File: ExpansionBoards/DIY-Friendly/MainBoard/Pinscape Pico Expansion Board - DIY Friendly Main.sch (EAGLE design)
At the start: 111 parts, among them IC1 UCC27524P, IC10 ULN2803A, IC11 SN74HC165N, IC12 SN74HC165N, IC13 SN74HC74NE4, IC14 PC827, IC15 S-80833CLY, IC16 SN74HC165N, IC18 SN74HC165N, IC2 UCC27524P, IC3 UCC27524P, IC4 UCC27524P, IC5 UCC27524P, IC6 UCC27524P, IC7 ULN2803A, IC8 ULN2803A, IC9 ULN2803A, J1 30316-6002HB, J10 215079-4, J11 640454-2, J13 640445-2, J14 SSQ-108-02-T-S-RA, J2 640445-6, J3 640445-5, J4 640445-9, J5 1-640456-0, J6 1-640456-0, J7 1-640456-0, J8 1-640456-0, J9 30308-6002HB, Q1 FDPF085N10A, Q10 FDPF085N10A, Q11 FDPF085N10A, Q12 FDPF085N10A, Q13 BC337-25, Q15 2N5195G, Q16 2N2222A, Q2 FDPF085N10A, Q3 FDPF085N10A, Q4 FDPF085N10A, Q5 FDPF085N10A, Q6 FDPF085N10A, Q7 FDPF085N10A, Q8 FDPF085N10A, Q9 FDPF085N10A

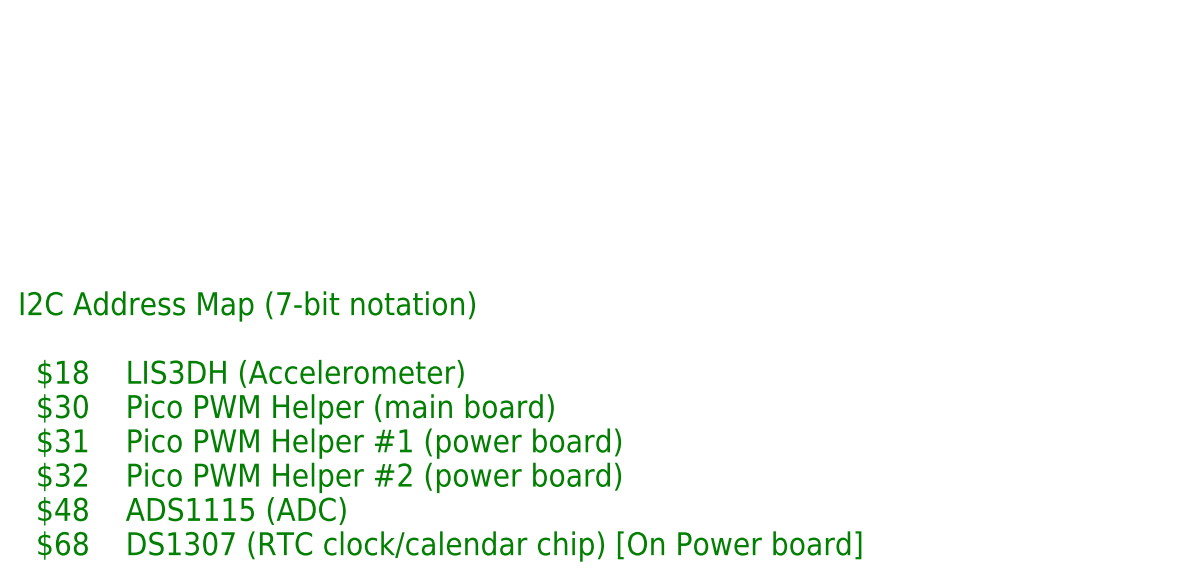
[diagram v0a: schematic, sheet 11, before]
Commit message: PCB parts lists (BOMs); power distro board edits
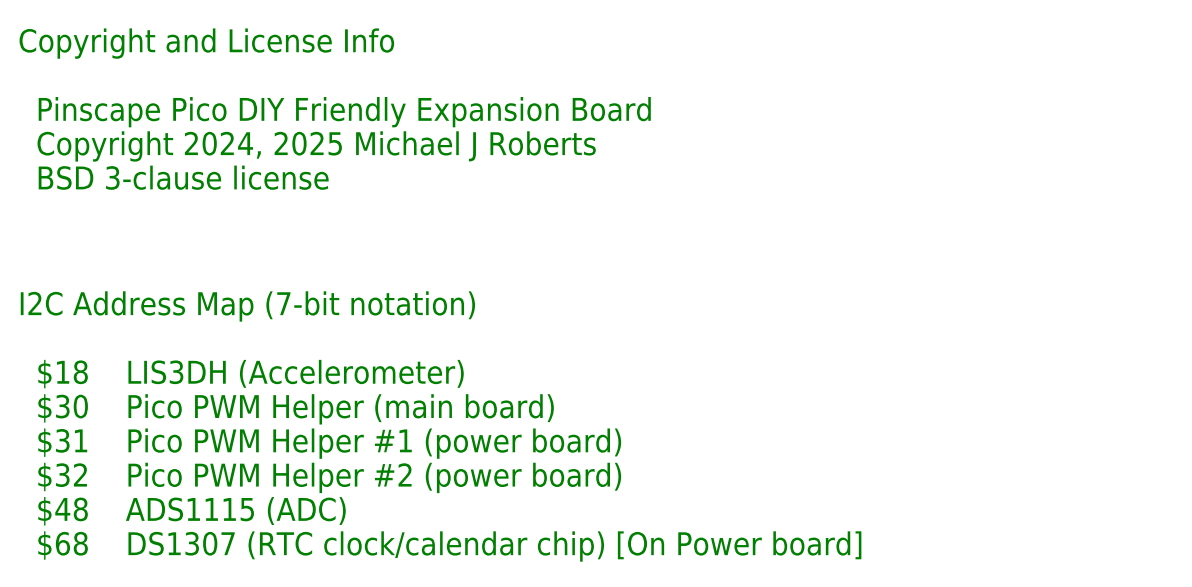
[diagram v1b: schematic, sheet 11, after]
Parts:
- C1, C10, C11, C13, C15, C18, C19, C3, C5, C7, C9: PARTNO 21RZ310-RC -> K104K15X7RF5TL2
- R10, R11: PARTNO 660-MFS1/4DCT52R47R0 -> MFR25SFTE52-10R
- R12, R13, R20, R22: PARTNO 660-MFS1/4DCT52R47R0 -> mfr-12frrf52-10k
- R26: PARTNO 660-MFS1/4DCT52R47R0 -> MF0204FTE52-1K
- R29, R30: PARTNO 660-MFS1/4DCT52R47R0 -> MFR25SFRF52-15K
- R9: PARTNO 660-MFS1/4DCT52R47R0 -> MFR-12FTE52-100R
- S1, S2: value (none) -> B3F-1000
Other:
- note added: "Copyright and License Info Pinscape Pico DIY Friendly Expansion Board Copyright 2024, 2025 Michael J Roberts BSD 3-clause license"
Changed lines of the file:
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@@
 <part name="GND47" library="supply1" deviceset="GND" device=""/>
 <part name="PICO1" library="RaspberryPi_Pico" deviceset="RPI_PICO_NO_DEBUG" device=""/>
-<part name="S1" library="switch-omron" deviceset="10-XX" device=""/>
+<part name="S1" library="switch-omron" deviceset="10-XX" device="" value="B3F-1000"/>
 <part name="JP1" library="pinhead" deviceset="PINHD-1X6" device=""/>
 <part name="JP2" library="pinhead" deviceset="PINHD-1X6" device=""/>
@@
 </part>
 <part name="C1" library="rcl" deviceset="C-US" device="025-024X044" value="100nF">
-<attribute name="PARTNO" value="21RZ310-RC"/>
+<attribute name="PARTNO" value="K104K15X7RF5TL2"/>
 </part>
 <part name="C2" library="rcl" deviceset="C-US" device="025-024X044" value="4.7uF">
@@
 </part>
 <part name="C3" library="rcl" deviceset="C-US" device="025-024X044" value="100nF">
-<attribute name="PARTNO" value="21RZ310-RC"/>
+<attribute name="PARTNO" value="K104K15X7RF5TL2"/>
 </part>
 <part name="C4" library="rcl" deviceset="C-US" device="025-024X044" value="4.7uF">
@@
 </part>
 <part name="C5" library="rcl" deviceset="C-US" device="025-024X044" value="100nF">
-<attribute name="PARTNO" value="21RZ310-RC"/>
+<attribute name="PARTNO" value="K104K15X7RF5TL2"/>
 </part>
 <part name="C6" library="rcl" deviceset="C-US" device="025-024X044" value="4.7uF">
@@
 </part>
 <part name="C7" library="rcl" deviceset="C-US" device="025-024X044" value="100nF">
-<attribute name="PARTNO" value="21RZ310-RC"/>
+<attribute name="PARTNO" value="K104K15X7RF5TL2"/>
 </part>
 <part name="C8" library="rcl" deviceset="C-US" device="025-024X044" value="4.7uF">
@@
 <part name="D1" library="SamacSys_Parts" deviceset="SB140-T" device=""/>
 <part name="R9" library="resistor" deviceset="R-US_" device="0204/7" value="100R">
-<attribute name="PARTNO" value="660-MFS1/4DCT52R47R0"/>
+<attribute name="PARTNO" value="MFR-12FTE52-100R"/>
 </part>
 <part name="LED2" library="SamacSys_Parts" deviceset="521-8559F" device=""/>
 <part name="R10" library="resistor" deviceset="R-US_" device="0204/7" value="10R">
-<attribute name="PARTNO" value="660-MFS1/4DCT52R47R0"/>
+<attribute name="PARTNO" value="MFR25SFTE52-10R"/>
 </part>
 <part name="R11" library="resistor" deviceset="R-US_" device="0204/7" value="10R">
-<attribute name="PARTNO" value="660-MFS1/4DCT52R47R0"/>
+<attribute name="PARTNO" value="MFR25SFTE52-10R"/>
 </part>
 <part name="R12" library="resistor" deviceset="R-US_" device="0204/7" value="10K">
-<attribute name="PARTNO" value="660-MFS1/4DCT52R47R0"/>
+<attribute name="PARTNO" value="mfr-12frrf52-10k"/>
 </part>
 <part name="R13" library="resistor" deviceset="R-US_" device="0204/7" value="10K">
-<attribute name="PARTNO" value="660-MFS1/4DCT52R47R0"/>
+<attribute name="PARTNO" value="mfr-12frrf52-10k"/>
 </part>
 <part name="C9" library="rcl" deviceset="C-US" device="025-024X044" value="100nF">
-<attribute name="PARTNO" value="21RZ310-RC"/>
+<attribute name="PARTNO" value="K104K15X7RF5TL2"/>
 </part>
 <part name="IC7" library="uln-udn" deviceset="ULN2803A" device="" value="ULN2803A"/>
@@
 </part>
 <part name="C11" library="rcl" deviceset="C-US" device="025-024X044" value="100nF">
-<attribute name="PARTNO" value="21RZ310-RC"/>
+<attribute name="PARTNO" value="K104K15X7RF5TL2"/>
 </part>
 <part name="C12" library="rcl" deviceset="C-US" device="025-024X044" value="4.7uF">
@@
 </part>
 <part name="C13" library="rcl" deviceset="C-US" device="025-024X044" value="100nF">
-<attribute name="PARTNO" value="21RZ310-RC"/>
+<attribute name="PARTNO" value="K104K15X7RF5TL2"/>
 </part>
 <part name="C14" library="rcl" deviceset="C-US" device="025-024X044" value="4.7uF">
@@
 <part name="IC15" library="SamacSys_Parts" deviceset="S-80833CLY-B2-U" device="TO92" value="S-80833CLY"/>
 <part name="C15" library="rcl" deviceset="C-US" device="025-024X044" value="100nF">
-<attribute name="PARTNO" value="21RZ310-RC"/>
+<attribute name="PARTNO" value="K104K15X7RF5TL2"/>
 </part>
 <part name="R18" library="resistor" deviceset="R-US_" device="0204/7" value="240R">
@@
 </part>
 <part name="R20" library="resistor" deviceset="R-US_" device="0204/7" value="10K">
-<attribute name="PARTNO" value="660-MFS1/4DCT52R47R0"/>
+<attribute name="PARTNO" value="mfr-12frrf52-10k"/>
 </part>
 <part name="R21" library="resistor" deviceset="R-US_" device="0204/7" value="360R">
@@
 </part>
 <part name="R22" library="resistor" deviceset="R-US_" device="0204/7" value="10K">
-<attribute name="PARTNO" value="660-MFS1/4DCT52R47R0"/>
+<attribute name="PARTNO" value="mfr-12frrf52-10k"/>
 </part>
 <part name="J13" library="SamacSys_Parts" deviceset="640445-2" device=""/>
@@
 <part name="IC11" library="SamacSys_Parts" deviceset="SN74HC165N" device=""/>
 <part name="C10" library="rcl" deviceset="C-US" device="025-024X044" value="100nF">
-<attribute name="PARTNO" value="21RZ310-RC"/>
+<attribute name="PARTNO" value="K104K15X7RF5TL2"/>
 </part>
 <part name="IC12" library="SamacSys_Parts" deviceset="SN74HC165N" device=""/>
 <part name="C18" library="rcl" deviceset="C-US" device="025-024X044" value="100nF">
-<attribute name="PARTNO" value="21RZ310-RC"/>
+<attribute name="PARTNO" value="K104K15X7RF5TL2"/>
 </part>
 <part name="IC16" library="SamacSys_Parts" deviceset="SN74HC165N" device=""/>
 <part name="C19" library="rcl" deviceset="C-US" device="025-024X044" value="100nF">
-<attribute name="PARTNO" value="21RZ310-RC"/>
+<attribute name="PARTNO" value="K104K15X7RF5TL2"/>
 </part>
 <part name="IC18" library="SamacSys_Parts" deviceset="SN74HC165N" device=""/>
@@
 <part name="R25" library="SamacSys_Parts - backup" deviceset="4609X-101-122LF" device="" value="4609X-101-103F"/>
 <part name="R26" library="resistor" deviceset="R-US_" device="0204/7" value="1K">
-<attribute name="PARTNO" value="660-MFS1/4DCT52R47R0"/>
+<attribute name="PARTNO" value="MF0204FTE52-1K"/>
 </part>
 <part name="R28" library="resistor" deviceset="R-US_" device="0204/7" value="22K">
@@
 <part name="GND4" library="supply1" deviceset="GND" device=""/>
 <part name="R29" library="resistor" deviceset="R-US_" device="0204/7" value="15K">
-<attribute name="PARTNO" value="660-MFS1/4DCT52R47R0"/>
+<attribute name="PARTNO" value="MFR25SFRF52-15K"/>
 </part>
 <part name="R30" library="resistor" deviceset="R-US_" device="0204/7" value="15K">
-<attribute name="PARTNO" value="660-MFS1/4DCT52R47R0"/>
+<attribute name="PARTNO" value="MFR25SFRF52-15K"/>
 </part>
 <part name="Q15" library="SamacSys_Parts" deviceset="2N5195G" device=""/>
@@
 <attribute name="PARTNO" value="660-MFS1/4DCT52R47R0"/>
 </part>
-<part name="S2" library="switch-omron" deviceset="10-XX" device=""/>
+<part name="S2" library="switch-omron" deviceset="10-XX" device="" value="B3F-1000"/>
 <part name="GND7" library="supply1" deviceset="GND" device=""/>
 <part name="J14" library="SamacSys_Parts" deviceset="SSQ-108-02-T-S-RA" device=""/>
@@
   $48    ADS1115 (ADC)
   $68    DS1307 (RTC clock/calendar chip) [On Power board]</text>
+<text x="2.54" y="43.18" size="2.54" layer="91">Copyright and License Info
+  Pinscape Pico DIY Friendly Expansion Board
+  Copyright 2024, 2025 Michael J Roberts
+  BSD 3-clause license</text>
 </plain>
 <instances>

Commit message: BOM tweaks
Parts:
- Q1, Q10, Q11, Q12, Q3, Q4, Q5, Q6, Q7, Q8, Q9: value FDPF085N10A -> STP19NF20
- R1, R14, R15, R16, R17, R2, R3, R4, R5, R6, R7, R8: value 4R7 -> 200R
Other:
- note added: "Note: Gate resistor value of 200 Ohms is chosen to protect UCC27524P against damage due to excessive power dissipation during PWM switching. In principle, the gate resistor is primarily to suppress ringing, which only requires a small resistor in the 5 to 10 Ohm range. But practical testing shows that UCC27524P is vulnerable to overload when used with MOSFETs with high input capacitance (C[ISS]).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"
- note added: "Note: Many similar MOSFETs are available. Choose a TO-220 package with G-D-S pin order and Absolute Maximum V[gs] of at least +/- 20V. Low input capacitance (C[ISS]) and total gate charge (Q[g]) are also desirable. Beyond that, choose based on the required Absolute Maximum values for drain current and voltage (I[D], V[DS]), which determine the limits for the output devices you can connect to the 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"
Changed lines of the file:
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@@
 <part name="IC1" library="SamacSys_Parts" deviceset="UCC27524P" device=""/>
 <part name="J4" library="SamacSys_Parts" deviceset="640445-9" device=""/>
-<part name="Q1" library="BUK7575" deviceset="BUK7575-55A" device="" value="FDPF085N10A">
+<part name="Q1" library="BUK7575" deviceset="BUK7575-55A" device="" value="STP19NF20">
 <attribute name="PARTNO" value="FDPF085N10A"/>
 </part>
-<part name="R1" library="resistor" deviceset="R-US_" device="0204/5" value="4R7">
+<part name="R1" library="resistor" deviceset="R-US_" device="0204/5" value="200R">
 <attribute name="PARTNO" value="660-MFS1/4DCT52R47R0"/>
 </part>
@@
 <attribute name="PARTNO" value="FDPF085N10A"/>
 </part>
-<part name="R2" library="resistor" deviceset="R-US_" device="0204/5" value="4R7">
+<part name="R2" library="resistor" deviceset="R-US_" device="0204/5" value="200R">
 <attribute name="PARTNO" value="660-MFS1/4DCT52R47R0"/>
 </part>
@@
 </part>
 <part name="IC2" library="SamacSys_Parts" deviceset="UCC27524P" device=""/>
-<part name="Q3" library="BUK7575" deviceset="BUK7575-55A" device="" value="FDPF085N10A">
+<part name="Q3" library="BUK7575" deviceset="BUK7575-55A" device="" value="STP19NF20">
 <attribute name="PARTNO" value="FDPF085N10A"/>
 </part>
-<part name="R3" library="resistor" deviceset="R-US_" device="0204/5" value="4R7">
+<part name="R3" library="resistor" deviceset="R-US_" device="0204/5" value="200R">
 <attribute name="PARTNO" value="660-MFS1/4DCT52R47R0"/>
 </part>
-<part name="Q4" library="BUK7575" deviceset="BUK7575-55A" device="" value="FDPF085N10A">
+<part name="Q4" library="BUK7575" deviceset="BUK7575-55A" device="" value="STP19NF20">
 <attribute name="PARTNO" value="FDPF085N10A"/>
 </part>
-<part name="R4" library="resistor" deviceset="R-US_" device="0204/5" value="4R7">
+<part name="R4" library="resistor" deviceset="R-US_" device="0204/5" value="200R">
 <attribute name="PARTNO" value="660-MFS1/4DCT52R47R0"/>
 </part>
@@
 </part>
 <part name="IC3" library="SamacSys_Parts" deviceset="UCC27524P" device=""/>
-<part name="Q5" library="BUK7575" deviceset="BUK7575-55A" device="" value="FDPF085N10A">
+<part name="Q5" library="BUK7575" deviceset="BUK7575-55A" device="" value="STP19NF20">
 <attribute name="PARTNO" value="FDPF085N10A"/>
 </part>
-<part name="R5" library="resistor" deviceset="R-US_" device="0204/5" value="4R7">
+<part name="R5" library="resistor" deviceset="R-US_" device="0204/5" value="200R">
 <attribute name="PARTNO" value="660-MFS1/4DCT52R47R0"/>
 </part>
-<part name="Q6" library="BUK7575" deviceset="BUK7575-55A" device="" value="FDPF085N10A">
+<part name="Q6" library="BUK7575" deviceset="BUK7575-55A" device="" value="STP19NF20">
 <attribute name="PARTNO" value="FDPF085N10A"/>
 </part>
-<part name="R6" library="resistor" deviceset="R-US_" device="0204/5" value="4R7">
+<part name="R6" library="resistor" deviceset="R-US_" device="0204/5" value="200R">
 <attribute name="PARTNO" value="660-MFS1/4DCT52R47R0"/>
 </part>
@@
 </part>
 <part name="IC4" library="SamacSys_Parts" deviceset="UCC27524P" device=""/>
-<part name="Q7" library="BUK7575" deviceset="BUK7575-55A" device="" value="FDPF085N10A">
+<part name="Q7" library="BUK7575" deviceset="BUK7575-55A" device="" value="STP19NF20">
 <attribute name="PARTNO" value="FDPF085N10A"/>
 </part>
-<part name="R7" library="resistor" deviceset="R-US_" device="0204/5" value="4R7">
+<part name="R7" library="resistor" deviceset="R-US_" device="0204/5" value="200R">
 <attribute name="PARTNO" value="660-MFS1/4DCT52R47R0"/>
 </part>
-<part name="Q8" library="BUK7575" deviceset="BUK7575-55A" device="" value="FDPF085N10A">
+<part name="Q8" library="BUK7575" deviceset="BUK7575-55A" device="" value="STP19NF20">
 <attribute name="PARTNO" value="FDPF085N10A"/>
 </part>
-<part name="R8" library="resistor" deviceset="R-US_" device="0204/5" value="4R7">
+<part name="R8" library="resistor" deviceset="R-US_" device="0204/5" value="200R">
 <attribute name="PARTNO" value="660-MFS1/4DCT52R47R0"/>
 </part>
@@
 <part name="J12" library="pinhead" deviceset="PINHD-1X3" device=""/>
 <part name="IC5" library="SamacSys_Parts" deviceset="UCC27524P" device=""/>
-<part name="Q9" library="BUK7575" deviceset="BUK7575-55A" device="" value="FDPF085N10A">
+<part name="Q9" library="BUK7575" deviceset="BUK7575-55A" device="" value="STP19NF20">
 <attribute name="PARTNO" value="FDPF085N10A"/>
 </part>
-<part name="R14" library="resistor" deviceset="R-US_" device="0204/5" value="4R7">
+<part name="R14" library="resistor" deviceset="R-US_" device="0204/5" value="200R">
 <attribute name="PARTNO" value="660-MFS1/4DCT52R47R0"/>
 </part>
-<part name="Q10" library="BUK7575" deviceset="BUK7575-55A" device="" value="FDPF085N10A">
+<part name="Q10" library="BUK7575" deviceset="BUK7575-55A" device="" value="STP19NF20">
 <attribute name="PARTNO" value="FDPF085N10A"/>
 </part>
-<part name="R15" library="resistor" deviceset="R-US_" device="0204/5" value="4R7">
+<part name="R15" library="resistor" deviceset="R-US_" device="0204/5" value="200R">
 <attribute name="PARTNO" value="660-MFS1/4DCT52R47R0"/>
 </part>
@@
 <part name="J3" library="SamacSys_Parts" deviceset="640445-5" device=""/>
 <part name="IC6" library="SamacSys_Parts" deviceset="UCC27524P" device=""/>
-<part name="Q11" library="BUK7575" deviceset="BUK7575-55A" device="" value="FDPF085N10A">
+<part name="Q11" library="BUK7575" deviceset="BUK7575-55A" device="" value="STP19NF20">
 <attribute name="PARTNO" value="FDPF085N10A"/>
 </part>
-<part name="R16" library="resistor" deviceset="R-US_" device="0204/5" value="4R7">
+<part name="R16" library="resistor" deviceset="R-US_" device="0204/5" value="200R">
 <attribute name="PARTNO" value="660-MFS1/4DCT52R47R0"/>
 </part>
-<part name="Q12" library="BUK7575" deviceset="BUK7575-55A" device="" value="FDPF085N10A">
+<part name="Q12" library="BUK7575" deviceset="BUK7575-55A" device="" value="STP19NF20">
 <attribute name="PARTNO" value="FDPF085N10A"/>
 </part>
-<part name="R17" library="resistor" deviceset="R-US_" device="0204/5" value="4R7">
+<part name="R17" library="resistor" deviceset="R-US_" device="0204/5" value="200R">
 <attribute name="PARTNO" value="660-MFS1/4DCT52R47R0"/>
 </part>
@@
 <text x="132.08" y="175.26" size="1.778" layer="91" rot="MR0" align="center">High-power MOSFET drivers</text>
 <text x="36.322" y="119.38" size="1.778" layer="91" align="center-left">KEY</text>
+<text x="190.5" y="76.2" size="2.032" layer="91" align="top-left">Note: Gate resistor value of 200 Ohms is chosen
+to protect UCC27524P against damage due to
+excessive power dissipation during PWM switching.
+In principle, the gate resistor is primarily to suppress
+ringing, which only requires a small resistor in the 5
+to 10 Ohm range.  But practical testing shows that
+UCC27524P is vulnerable to overload when used
+with MOSFETs with high input capacitance (C[ISS]).
+200 Ohms appears safe for common FETs such as
+IRF540N.  Higher resistor values also increase
+MOSFET heating during PWM operation, due to
+increased switching time, so increasing this value
+above 200 Ohms should be avoided.
+</text>
+<text x="190.5" y="30.48" size="2.032" layer="91" align="top-left">Note: Many similar MOSFETs are available.  Choose
+a TO-220 package with G-D-S pin order and Absolute
+Maximum V[gs] of at least +/- 20V.  Low input
+capacitance (C[ISS]) and total gate charge (Q[g]) are
+also desirable.  Beyond that, choose based on the
+required Absolute Maximum values for drain current
+and voltage (I[D], V[DS]), which determine the limits
+for the output devices you can connect to the ports.</text>
 </plain>
 <instances>
